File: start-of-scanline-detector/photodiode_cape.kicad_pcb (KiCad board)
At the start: 2 copper layers, 28.5 x 17.1 mm, 19 parts, among them J1 S3B-PH-K-S, U1 MIC920, U2 MIC920

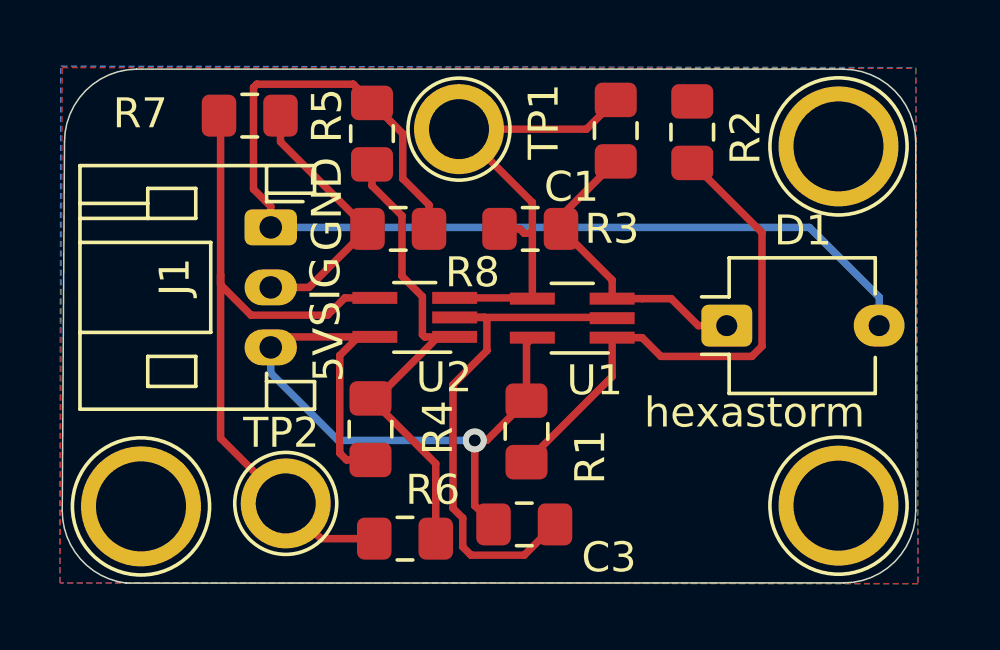
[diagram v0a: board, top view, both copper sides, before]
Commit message: fixed xpo pin connection
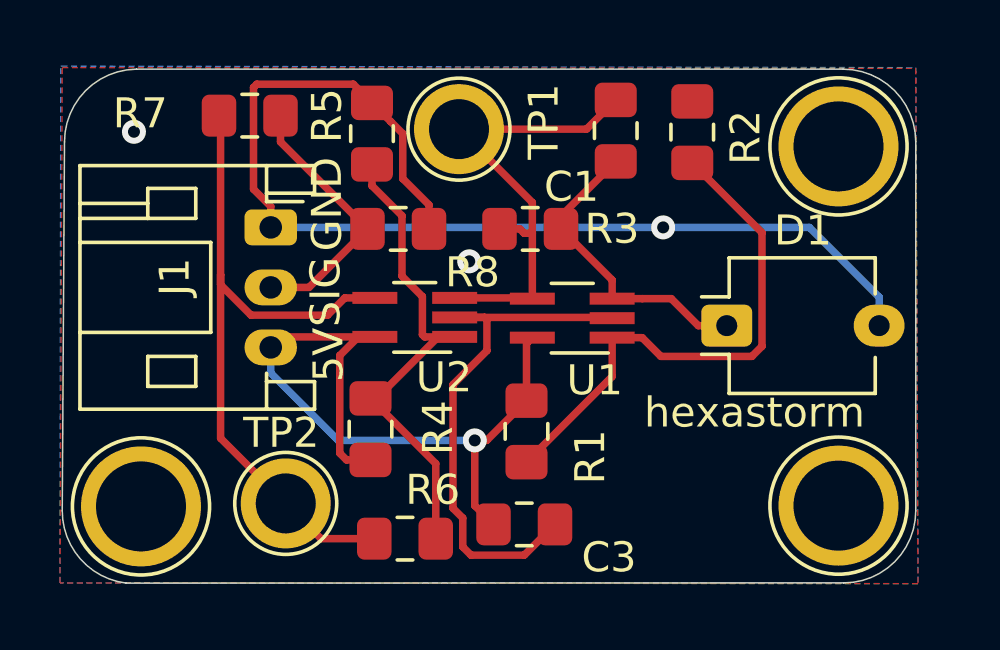
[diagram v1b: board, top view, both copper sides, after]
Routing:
- net GND: vias 0 -> 3
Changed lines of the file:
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@@
-(kicad_pcb (version 20171130) (host pcbnew "(5.1.2)-2")
+(kicad_pcb (version 20171130) (host pcbnew "(5.1.0)-1")
   (general
     (thickness 1.6)
     (drawings 12)
-    (tracks 102)
+    (tracks 106)
     (zones 0)
     (modules 19)
@@
     (pcbplotparams
       (layerselection 0x010fc_ffffffff)
-      (usegerberextensions false)
+      (usegerberextensions true)
       (usegerberattributes false)
       (usegerberadvancedattributes false)
@@
       (outputformat 1)
       (mirror false)
-      (drillshape 1)
+      (drillshape 0)
       (scaleselection 1)
-      (outputdirectory ""))
+      (outputdirectory "gerber/"))
   )
   (net 0 "")
@@
   (segment (start 84.53 30.15) (end 84.53 31.1) (width 0.25) (layer B.Cu) (net 3))
   (segment (start 82.205 27.825) (end 84.53 30.15) (width 0.25) (layer B.Cu) (net 3))
-  (segment (start 64.25 27.825) (end 82.205 27.825) (width 0.25) (layer B.Cu) (net 3))
+  (segment (start 64.25 27.825) (end 77.331 27.825) (width 0.25) (layer B.Cu) (net 3))
+  (segment (start 77.331 27.825) (end 82.205 27.825) (width 0.25) (layer B.Cu) (net 3))
+  (via (at 77.331 27.825) (size 0.8) (drill 0.4) (layers F.Cu B.Cu) (net 3))
+  (via (at 59.69 24.638) (size 0.8) (drill 0.4) (layers F.Cu B.Cu) (net 3))
+  (via (at 70.866 28.956) (size 0.8) (drill 0.4) (layers F.Cu B.Cu) (net 3))
   (via (at 71.05 34.925) (size 0.8) (drill 0.4) (layers F.Cu B.Cu) (net 4))
   (segment (start 68.27 31.475) (end 67.72 31.475) (width 0.25) (layer F.Cu) (net 4))

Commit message: updated 3D renders
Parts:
- D1: footprint OptoDevice:Osram_DIL2_4.3x4.65mm_P5.08mm -> start-of-scanline-detector:Osram_DIL2_4.3x4.65mm_P5.08mm

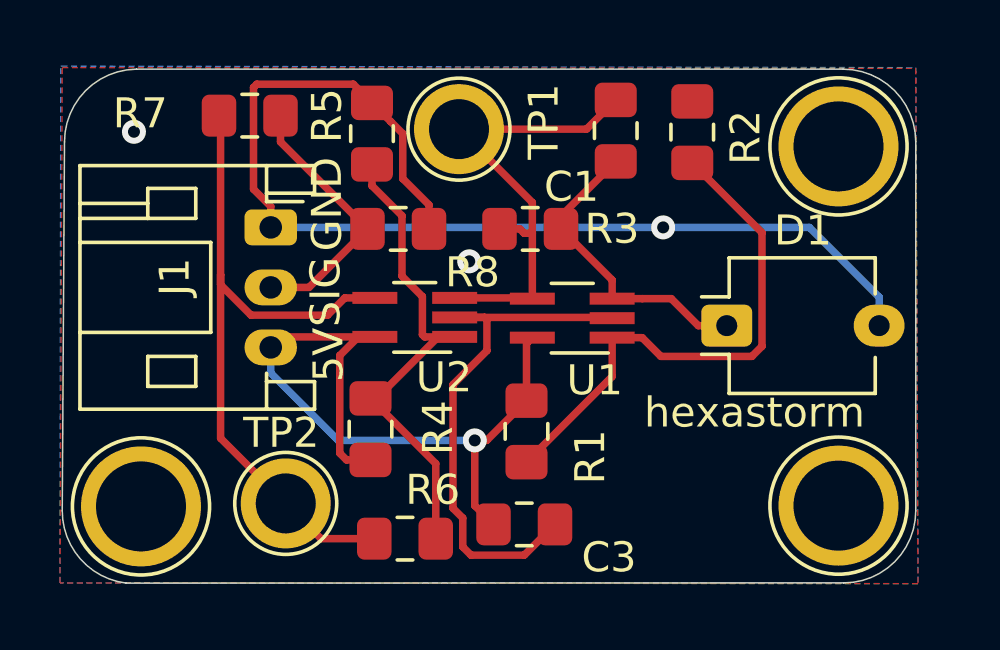
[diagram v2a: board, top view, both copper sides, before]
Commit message: changed most cables to flatex or jumper wire moved from 1 diode to 2 diodes added spi readout chip for photodiode photodiode is now surface mount
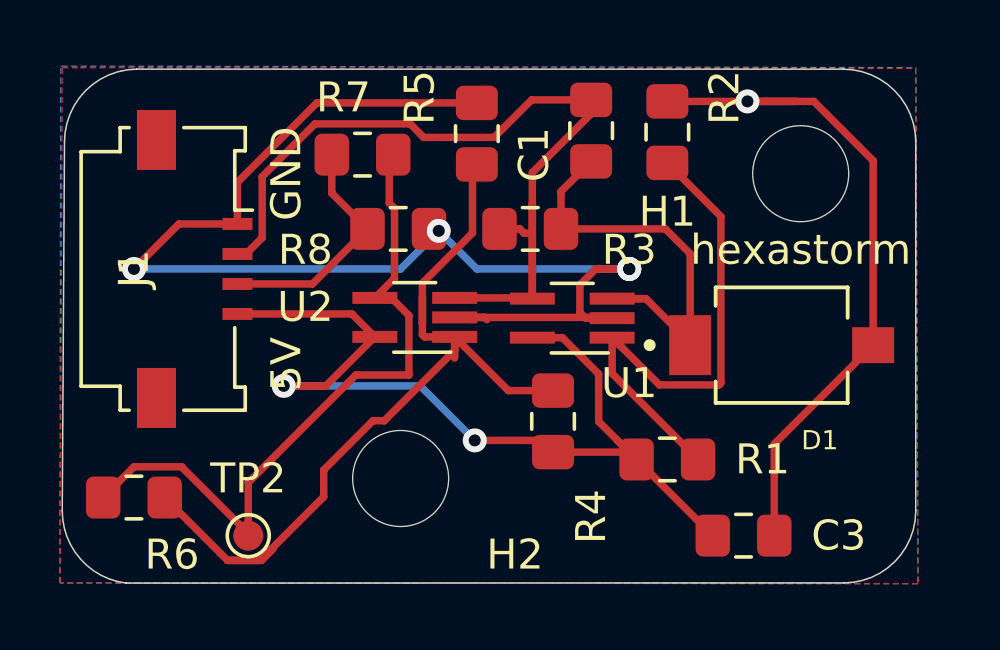
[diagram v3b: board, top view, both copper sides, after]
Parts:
- removed REF** (x3): TestPoint_Plated_Hole_D3.0mm, TestPoint:TestPoint_Plated_Hole_D3.0mm
- removed TP1: vPhoto, TestPoint:TestPoint_Plated_Hole_D2.0mm
- added H1: MountingHole, MountingHole:MountingHole_3.2mm_M3, F.Cu at (81.9, 26.0)
- added H2: MountingHole, MountingHole:MountingHole_3.2mm_M3, F.Cu at (68.6, 36.2)
- D1: value BPW34 -> BPW_34_S-Z; footprint start-of-scanline-detector:Osram_DIL2_4.3x4.65mm_P5.08mm -> start-of-scanline-detector:DIO_BPW_34_S-Z
- J1: value S3B-PH-K-S -> FPC molex 4 pin; footprint Connector_JST:JST_PH_S3B-PH-K_1x03_P2.00mm_Horizontal -> Connector_FFC-FPC:Molex_200528-0040_1x04-1MP_P1.00mm_Horizontal
- TP2: footprint TestPoint:TestPoint_Plated_Hole_D2.0mm -> TestPoint:TestPoint_Pad_D1.0mm
- moved R6 9.14 mm to (59.7, 36.8)
- moved C3 7.32 mm to (80.0, 38.1)
- moved R4 6.09 mm to (73.7, 34.3)
- moved R1 4.79 mm to (77.5, 35.6), turned to 180 degrees
- moved R7 3.98 mm to (67.3, 25.4), turned to 0 degrees
- moved R5 3.50 mm to (71.1, 24.7)
- moved J1 2.45 mm to (62.2, 29.2)
- moved D1 1.94 mm to (81.3, 31.8), turned to 180 degrees
- moved TP2 1.65 mm to (63.5, 38.1)
- moved R2 0.83 mm to (77.5, 24.6)
- moved C1 0.82 mm to (74.9, 24.6)
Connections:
- C1 pad 1: Net-(C1-Pad1) -> ANALOG
- J1 pad 2: HSync -> ANALOG
- J1 pad 3: +5V -> HSync
- R3 pad 2: Net-(C1-Pad1) -> ANALOG
- U1 pad 4: Net-(C1-Pad1) -> ANALOG
- U2 pad 3: Net-(C1-Pad1) -> ANALOG
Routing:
- net ANALOG: track 0.00 -> 29.9 mm
- net Net-(C1-Pad1): track 16.1 -> 0.00 mm
- net Net-(R4-Pad1): track 16.7 -> 29.8 mm
- net GND: track 55.0 -> 65.6 mm, vias 3 -> 5
- net +5V: track 26.3 -> 33.1 mm, vias 1 -> 2
- net Net-(C1-Pad2): track 10.2 -> 15.0 mm
- net HSync: track 9.13 -> 8.06 mm
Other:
- board text removed: "SIG"

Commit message: updated all boards
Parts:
- H1, H2: footprint MountingHole:MountingHole_3.2mm_M3 -> MountingHole:MountingHole_2.2mm_M2
- J1: footprint Connector_FFC-FPC:Molex_200528-0040_1x04-1MP_P1.00mm_Horizontal -> start-of-scanline-detector:Molex_200528-0040_1x04-1MP_P1.00mm_Horizontal
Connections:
- net HSync renamed DIGITAL
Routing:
- net Net-(R1-Pad1): track 18.1 -> 21.2 mm
- net Net-(R6-Pad1): track 23.3 -> 22.8 mm
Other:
- board text added: "ANA"
- board text added: "DIGI"

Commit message: new boards
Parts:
- H1, H2: footprint MountingHole:MountingHole_2.2mm_M2 -> MountingHole:MountingHole_2.7mm_M2.5
- moved C3 2.57 mm to (77.5, 37.7)
- moved R8 0.26 mm to (68.6, 27.6)
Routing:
- net GND: track 65.6 -> 42.7 mm, vias 5 -> 6
- net Net-(R1-Pad1): track 21.2 -> 18.3 mm
- net +5V: track 33.1 -> 32.2 mm
- net Net-(C1-Pad2): track 15.0 -> 14.1 mm
- net Net-(R4-Pad1): track 29.6 -> 28.9 mm
- net Net-(R6-Pad1): track 22.8 -> 22.3 mm

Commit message: updated bom
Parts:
- moved H1 10.2 mm to (82.6, 36.2)
- moved R2 7.00 mm to (78.9, 31.5), turned to 180 degrees
- moved D1 6.61 mm to (80.3, 25.2)
- moved TP2 1.85 mm to (64.2, 36.4)
- moved C3 1.20 mm to (76.8, 36.7)
- moved R6 1.11 mm to (60.7, 36.4)
- moved R1 1.09 mm to (76.8, 34.7)
- moved C1 0.12 mm to (74.9, 24.7)
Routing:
- net Net-(R1-Pad1): track 18.3 -> 6.37 mm
- net Net-(R4-Pad1): track 28.9 -> 24.4 mm
- net Net-(R6-Pad1): track 22.3 -> 19.5 mm
- net +5V: track 32.2 -> 29.7 mm
- net Net-(C1-Pad2): track 14.1 -> 15.4 mm
- net GND: vias 6 -> 5

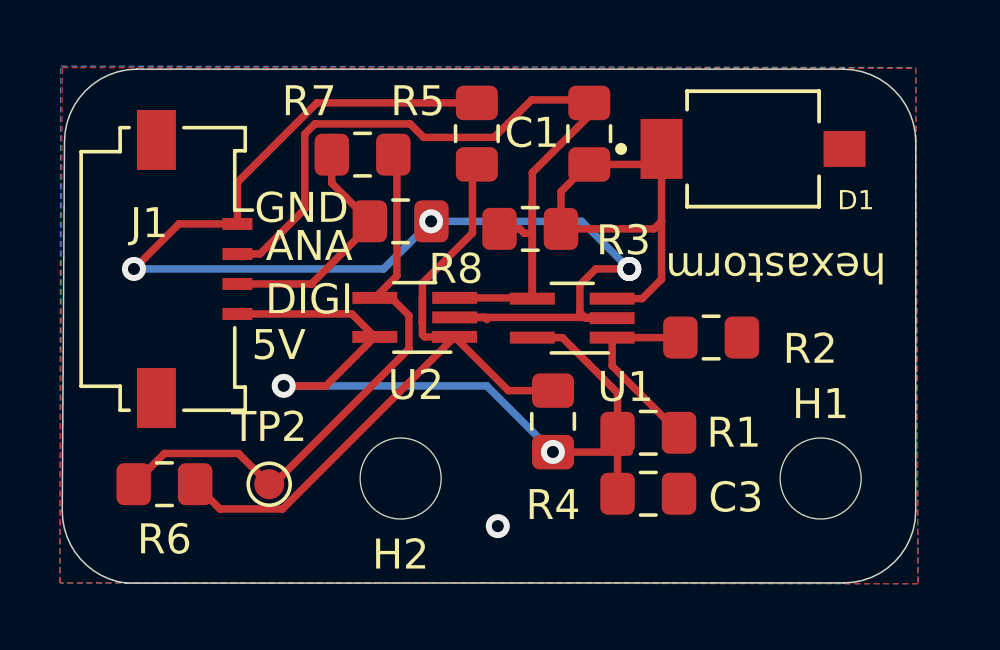
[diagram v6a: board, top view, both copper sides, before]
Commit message: positioned diode at edge
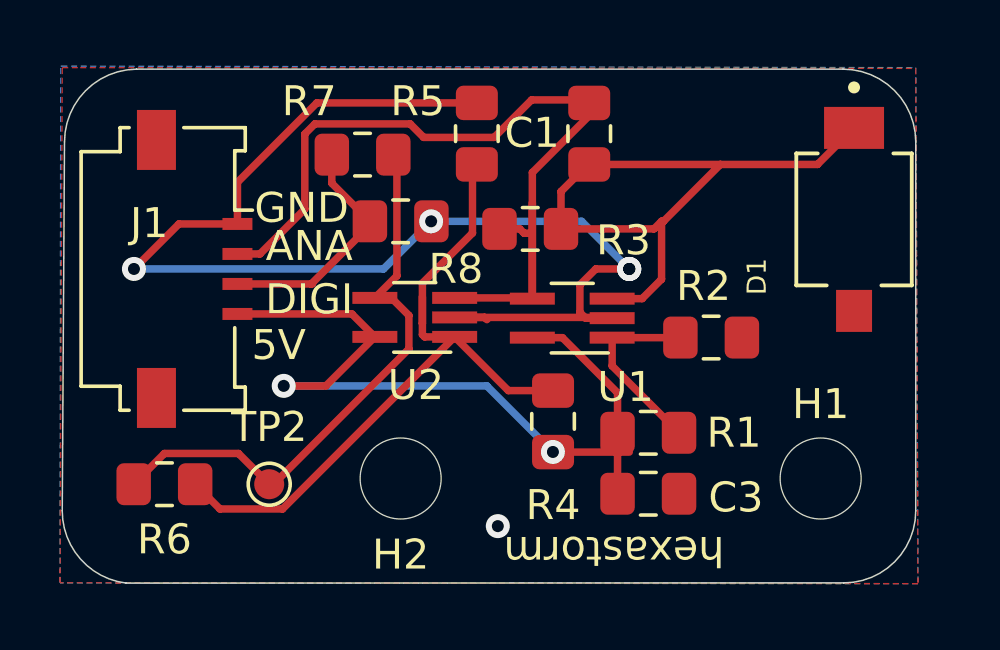
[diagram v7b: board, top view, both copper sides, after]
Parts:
- moved D1 4.10 mm to (83.7, 27.6), turned to 90 degrees
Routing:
- net Net-(C1-Pad2): track 15.4 -> 22.5 mm
